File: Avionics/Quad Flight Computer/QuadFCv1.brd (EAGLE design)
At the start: 63.5 x 38.1 mm, 111 parts, among them J1 10104111_MICROUSBAB, J2 1050270001, SW1 2-1437565-9, U1 TM4C123GH6PZ, U2 74LVC4245APW, U3 ATMEGA32U2-MU, U4 SPI_PPM, U5 MPU-6000, U6 HMC5883LSMD, U7 MS5611-01BA, U8 74AUP1G19GW, U9 S25FL127S, X1 HWB, Y1 32.768KHZ, Y2 AWSCR-20.00CW-T, Y3 PRQC16.00SR5010X000

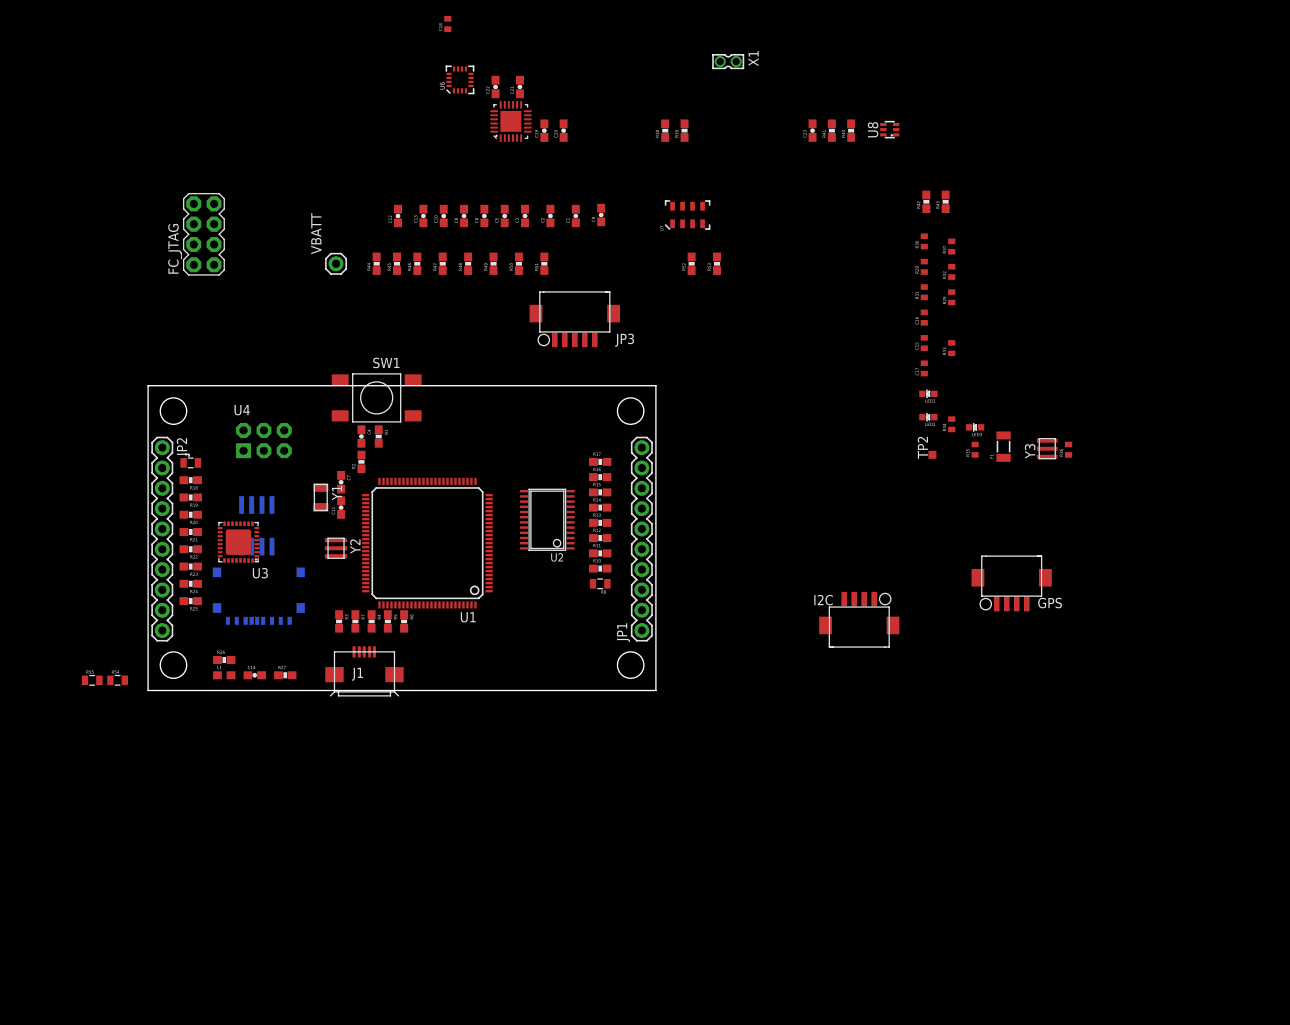
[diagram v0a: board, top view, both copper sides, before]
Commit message: Replaced all parts with 0402 packages to save board space.
I'm gonna need a smaller tweezers...
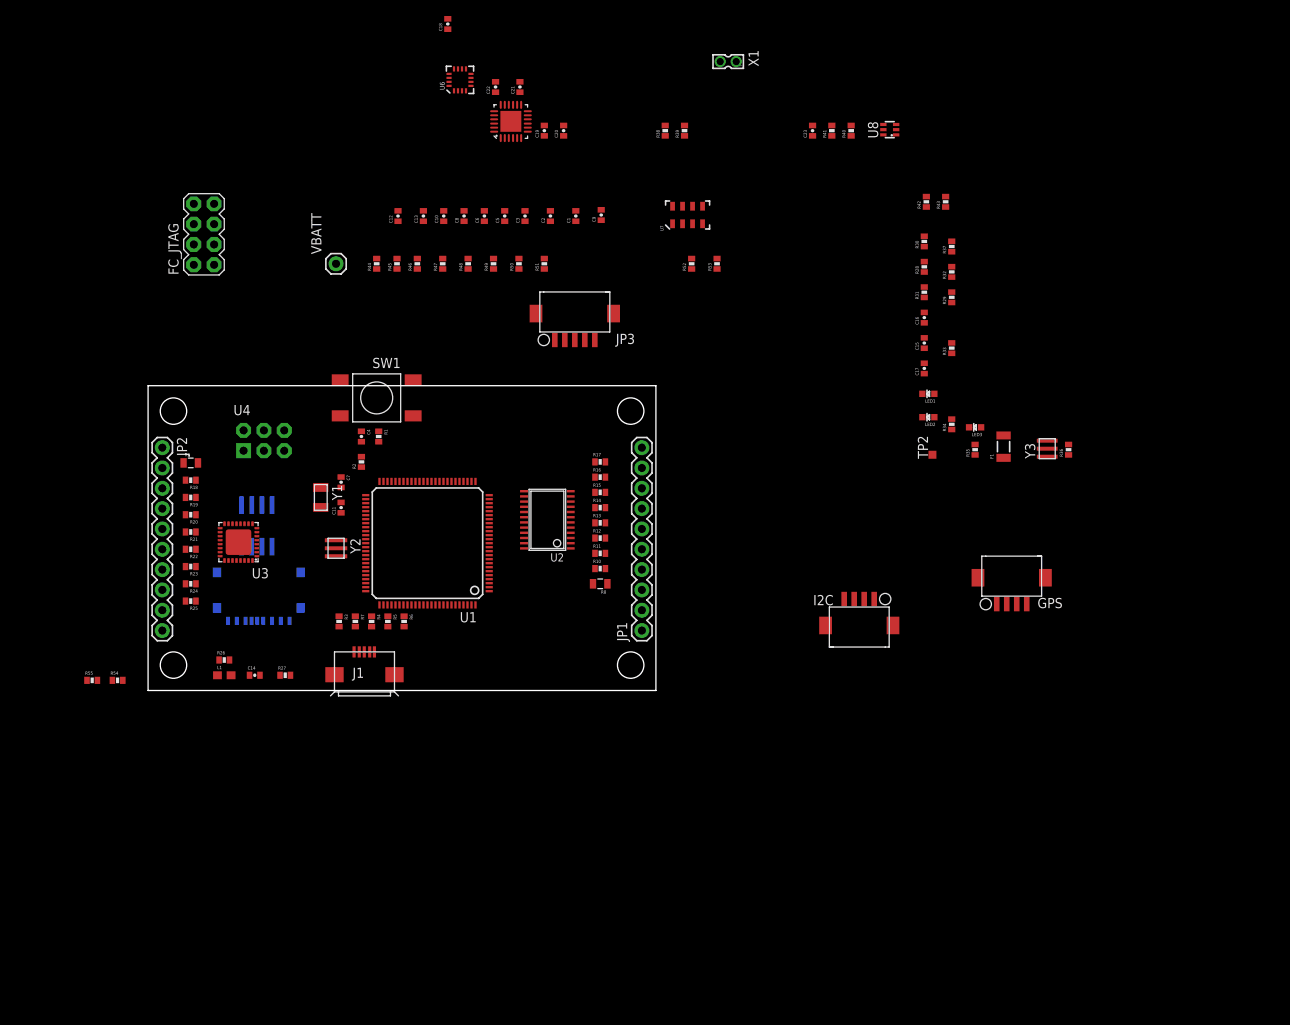
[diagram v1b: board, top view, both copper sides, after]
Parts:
- C1, C10, C11, C12, C13, C19, C2, C20, C21, C22, C23, C3, C4, C5, C6, C7, C8, C9: device SparkFun-Capacitors:0603-CAP -> SparkFun-Capacitors:0402-CAP
- C14: device SparkFun-Passives:0603-CAP -> SparkFun-Capacitors:0402-CAP
- C15, C16, C17, C18: device SparkFun:C0402 -> SparkFun-Capacitors:0402-CAP
- R1, R10, R11, R12, R13, R14, R15, R16, R17, R18, R19, R2, R20, R21, R22, R23, R24, R25, R26, R27, R38, R39, R40, R41: device SparkFun-Resistors:0603-RES -> SparkFun-Resistors:0402-RES
- R28, R29, R30, R31, R32, R33, R34, R35, R36, R37: device SparkFun:C0402 -> SparkFun-Resistors:0402-RES
- R3, R4, R42, R43, R44, R45, R46, R47, R48, R49, R5, R50, R51, R52, R53, R6, R7: device Shared Libraries:0603-RES -> SparkFun-Resistors:0402-RES
- R54, R55: value DNP -> 0; device SparkFun-Resistors:0805 -> SparkFun-Resistors:0402-RES
- R8, R9: value 0 -> DNP

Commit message: Added power management circuitry
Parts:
- added C24: 1uF, SparkFun-Capacitors:0603-CAP
- added C25, C26: 1u, SparkFun-Capacitors:0402-CAP
- added Q1, Q2, Q3: DMP2035U, Shared Libraries:SOT23
- added R56: 470K, Shared Libraries:0402-RES
- added U10: LTC4412, Shared Libraries:SOT23-6
- added U11: AP7215-33YG-13, Shared Libraries:SOT89
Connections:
- new net N$41: Q2.1, U10.5
- new net N$42: F1.1, Q1.3, Q3.2
- new net USB_EPEN: Q3.1
- new net USB_POWER_CONN_L: Q1.1, R56.1, U10.4
- new net VBUS: F1.2
- net 3.3V: now also C26.1, U11.3
- net 5V: now also C24.2, C25.1, Q1.2, Q2.2, R56.2, U10.6, U11.2, U11.2@1
- net 5VBATT: now also Q2.3, Q3.3, U10.1
- net GND: now also C24.1, C25.2, C26.2, U10.2, U10.3, U11.1
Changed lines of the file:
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@@
 <element name="R54" library="SparkFun-Resistors" package="0402-RES" value="0" x="-3.81" y="1.27"/>
 <element name="R55" library="SparkFun-Resistors" package="0402-RES" value="0" x="-6.985" y="1.27"/>
+<element name="Q1" library="Shared Libraries" package="SOT23" value="DMP2035U" x="-5.715" y="-4.445"/>
+<element name="Q2" library="Shared Libraries" package="SOT23" value="DMP2035U" x="-5.715" y="-12.065"/>
+<element name="Q3" library="Shared Libraries" package="SOT23" value="DMP2035U" x="-5.715" y="-19.685"/>
+<element name="U10" library="Shared Libraries" package="SOT23-6" value="LTC4412" x="-6.35" y="-26.67"/>
+<element name="R56" library="Shared Libraries" package="0402-RES" value="470K" x="-6.985" y="-31.115"/>
+<element name="C24" library="SparkFun-Capacitors" package="0603-CAP" value="1uF" x="-6.985" y="-33.655"/>
+<element name="U11" library="Shared Libraries" package="SOT89" value="AP7215-33YG-13" x="-13.97" y="-29.845"/>
+<element name="C25" library="SparkFun-Capacitors" package="0402-CAP" value="1u" x="-15.24" y="-36.83"/>
+<element name="C26" library="SparkFun-Capacitors" package="0402-CAP" value="1u" x="-15.24" y="-39.37"/>
 </elements>
 <signals>
@@
 <contactref element="R53" pad="2"/>
 <contactref element="I2C" pad="P1"/>
+<contactref element="U11" pad="3"/>
+<contactref element="C26" pad="1"/>
 <wire x1="83.058" y1="69.327" x2="91.91" y2="70.104" width="0" layer="19" extent="1-1"/>
 <wire x1="97.282" y1="61.737" x2="91.91" y2="70.104" width="0" layer="19" extent="1-1"/>
@@
 <wire x1="10.375" y1="1.905" x2="10.175" y2="3.81" width="0" layer="19" extent="1-1"/>
 <wire x1="5.715" y1="55.753" x2="34.417" y2="58.659" width="0" layer="19" extent="1-1"/>
+<wire x1="-12.471" y1="-31.826" x2="10.375" y2="1.905" width="0" layer="19" extent="1-1"/>
+<wire x1="-15.89" y1="-39.37" x2="-12.471" y2="-31.826" width="0" layer="19" extent="1-1"/>
 <wire x1="90.765" y1="11.43" x2="46.9932" y2="17.761" width="0" layer="19" extent="1-1"/>
 </signal>
@@
 <contactref element="GPS" pad="P4"/>
 <contactref element="I2C" pad="P4"/>
+<contactref element="U10" pad="2"/>
+<contactref element="U10" pad="3"/>
+<contactref element="C24" pad="1"/>
+<contactref element="C26" pad="2"/>
+<contactref element="U11" pad="1"/>
+<contactref element="C25" pad="2"/>
 <wire x1="83.058" y1="70.627" x2="93.51" y2="70.104" width="0" layer="19" extent="1-1"/>
 <wire x1="71.517" y1="78.613" x2="83.058" y2="70.627" width="0" layer="19" extent="1-1"/>
@@
 <wire x1="5.715" y1="60.833" x2="31.242" y2="59.959" width="0" layer="19" extent="1-1"/>
 <wire x1="5.715" y1="58.293" x2="5.715" y2="60.833" width="0" layer="19" extent="1-1"/>
+<wire x1="-5.4" y1="-27.82" x2="12.685" y2="1.905" width="0" layer="19" extent="1-1"/>
+<wire x1="-6.35" y1="-27.82" x2="-5.4" y2="-27.82" width="0" layer="19" extent="1-1"/>
+<wire x1="-7.835" y1="-33.655" x2="-6.35" y2="-27.82" width="0" layer="19" extent="1-1"/>
+<wire x1="-14.59" y1="-36.83" x2="-7.835" y2="-33.655" width="0" layer="19" extent="1-1"/>
+<wire x1="-14.59" y1="-39.37" x2="-14.59" y2="-36.83" width="0" layer="19" extent="1-1"/>
+<wire x1="-15.469" y1="-31.826" x2="-14.59" y2="-36.83" width="0" layer="19" extent="1-1"/>
 </signal>
 <signal name="5V">
@@
 <contactref element="R52" pad="2"/>
 <contactref element="R54" pad="2"/>
+<contactref element="Q2" pad="2"/>
+<contactref element="Q1" pad="2"/>
+<contactref element="U10" pad="6"/>
+<contactref element="R56" pad="2"/>
+<contactref element="C24" pad="2"/>
+<contactref element="C25" pad="1"/>
+<contactref element="U11" pad="2@1"/>
+<contactref element="U11" pad="2"/>
 <wire x1="100.457" y1="42.149" x2="100.457" y2="49.799" width="0" layer="19" extent="1-1"/>
 <wire x1="97.028" y1="42.784" x2="100.457" y2="42.149" width="0" layer="19" extent="1-1"/>
@@
 <wire x1="11.938" y1="32.512" x2="13.603" y2="18.292" width="0" layer="19" extent="1-1"/>
 <wire x1="-3.16" y1="1.27" x2="13.053" y2="16.242" width="0" layer="19" extent="1-1"/>
+<wire x1="-4.765" y1="-5.545" x2="-3.16" y2="1.27" width="0" layer="19" extent="1-1"/>
+<wire x1="-4.765" y1="-13.165" x2="-4.765" y2="-5.545" width="0" layer="19" extent="1-1"/>
+<wire x1="-7.3" y1="-25.52" x2="-4.765" y2="-13.165" width="0" layer="19" extent="1-1"/>
+<wire x1="-6.335" y1="-31.115" x2="-7.3" y2="-25.52" width="0" layer="19" extent="1-1"/>
+<wire x1="-6.135" y1="-33.655" x2="-6.335" y2="-31.115" width="0" layer="19" extent="1-1"/>
+<wire x1="-13.97" y1="-28.905" x2="-7.3" y2="-25.52" width="0" layer="19" extent="1-1"/>
+<wire x1="-13.97" y1="-31.572" x2="-13.97" y2="-28.905" width="0" layer="19" extent="1-1"/>
+<wire x1="-15.89" y1="-36.83" x2="-13.97" y2="-31.572" width="0" layer="19" extent="1-1"/>
 </signal>
 <signal name="N$1">
@@
 <contactref element="R9" pad="2"/>
 <contactref element="R55" pad="2"/>
+<contactref element="U10" pad="1"/>
+<contactref element="Q2" pad="3"/>
+<contactref element="Q3" pad="3"/>
 <wire x1="-6.335" y1="1.27" x2="6.234" y2="28.448" width="0" layer="19" extent="1-1"/>
+<wire x1="-5.715" y1="-10.965" x2="-6.335" y2="1.27" width="0" layer="19" extent="1-1"/>
+<wire x1="-5.715" y1="-18.585" x2="-5.715" y2="-10.965" width="0" layer="19" extent="1-1"/>
+<wire x1="-7.3" y1="-27.82" x2="-5.715" y2="-18.585" width="0" layer="19" extent="1-1"/>
+</signal>
+<signal name="N$41">
+<contactref element="Q2" pad="1"/>
+<contactref element="U10" pad="5"/>
+<wire x1="-6.665" y1="-13.165" x2="-6.35" y2="-25.52" width="0" layer="19" extent="1-1"/>
+</signal>
+<signal name="USB_POWER_CONN_L">
+<contactref element="U10" pad="4"/>
+<contactref element="Q1" pad="1"/>
+<contactref element="R56" pad="1"/>
+<wire x1="-5.4" y1="-25.52" x2="-7.635" y2="-31.115" width="0" layer="19" extent="1-1"/>
+<wire x1="-6.665" y1="-5.545" x2="-5.4" y2="-25.52" width="0" layer="19" extent="1-1"/>
+</signal>
+<signal name="USB_EPEN">
+<contactref element="Q3" pad="1"/>
+</signal>
+<signal name="VBUS">
+<contactref element="F1" pad="2"/>
+</signal>
+<signal name="N$42">
+<contactref element="F1" pad="1"/>
+<contactref element="Q1" pad="3"/>
+<contactref element="Q3" pad="2"/>
+<wire x1="-5.715" y1="-3.345" x2="106.934" y2="29.08" width="0" layer="19" extent="1-1"/>
+<wire x1="-4.765" y1="-20.785" x2="-5.715" y2="-3.345" width="0" layer="19" extent="1-1"/>
 </signal>
 </signals>

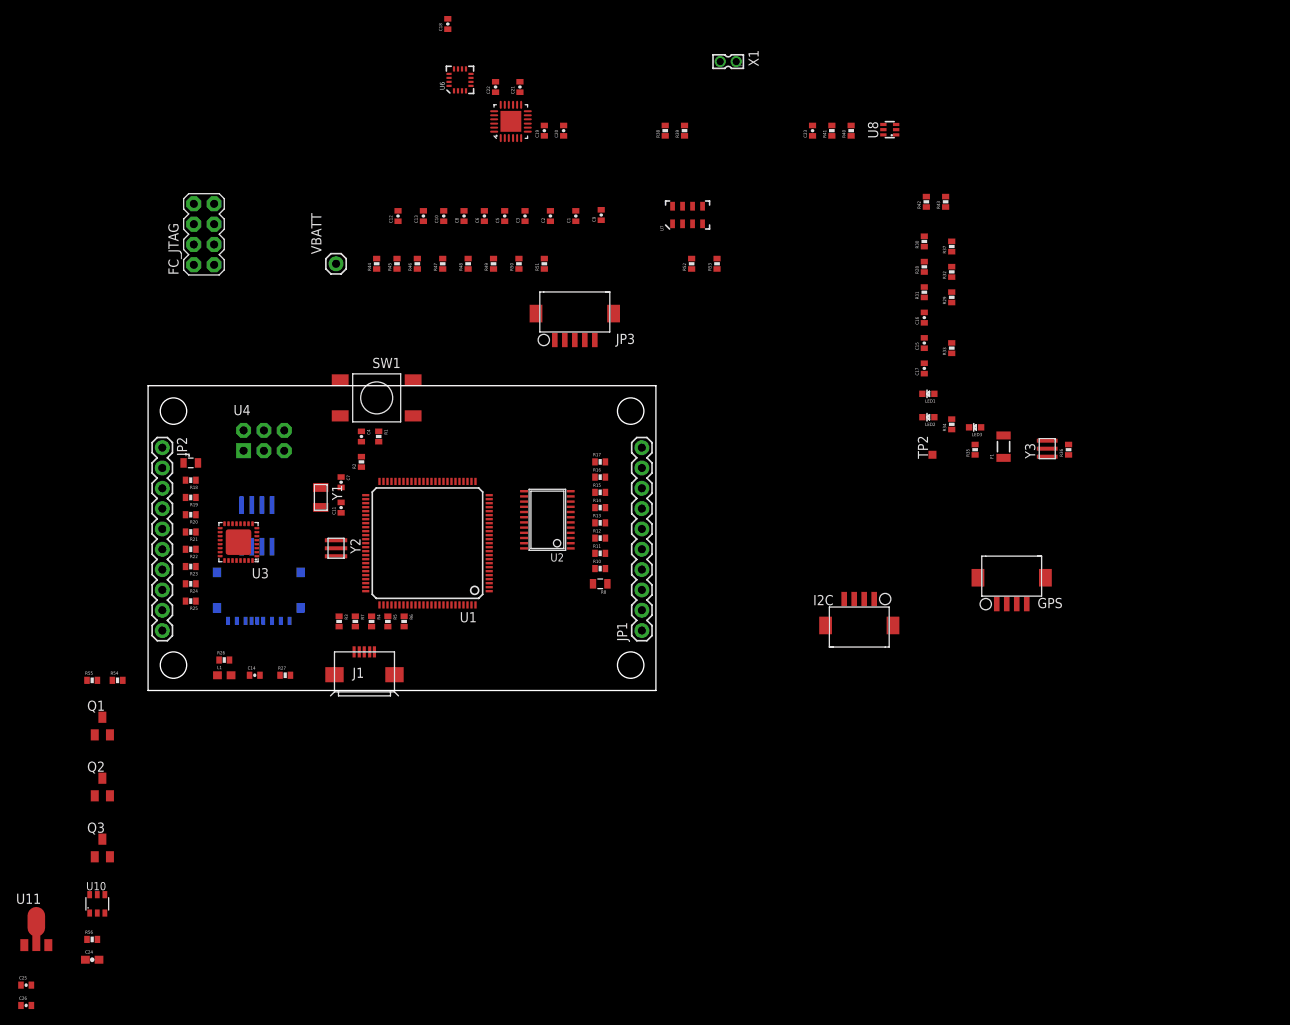
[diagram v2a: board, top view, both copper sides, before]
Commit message: Changed form factor of FC to be 1.95"x1.95" to be compliant with the power distribution board. Makes stacking and interconnectivity simpler.
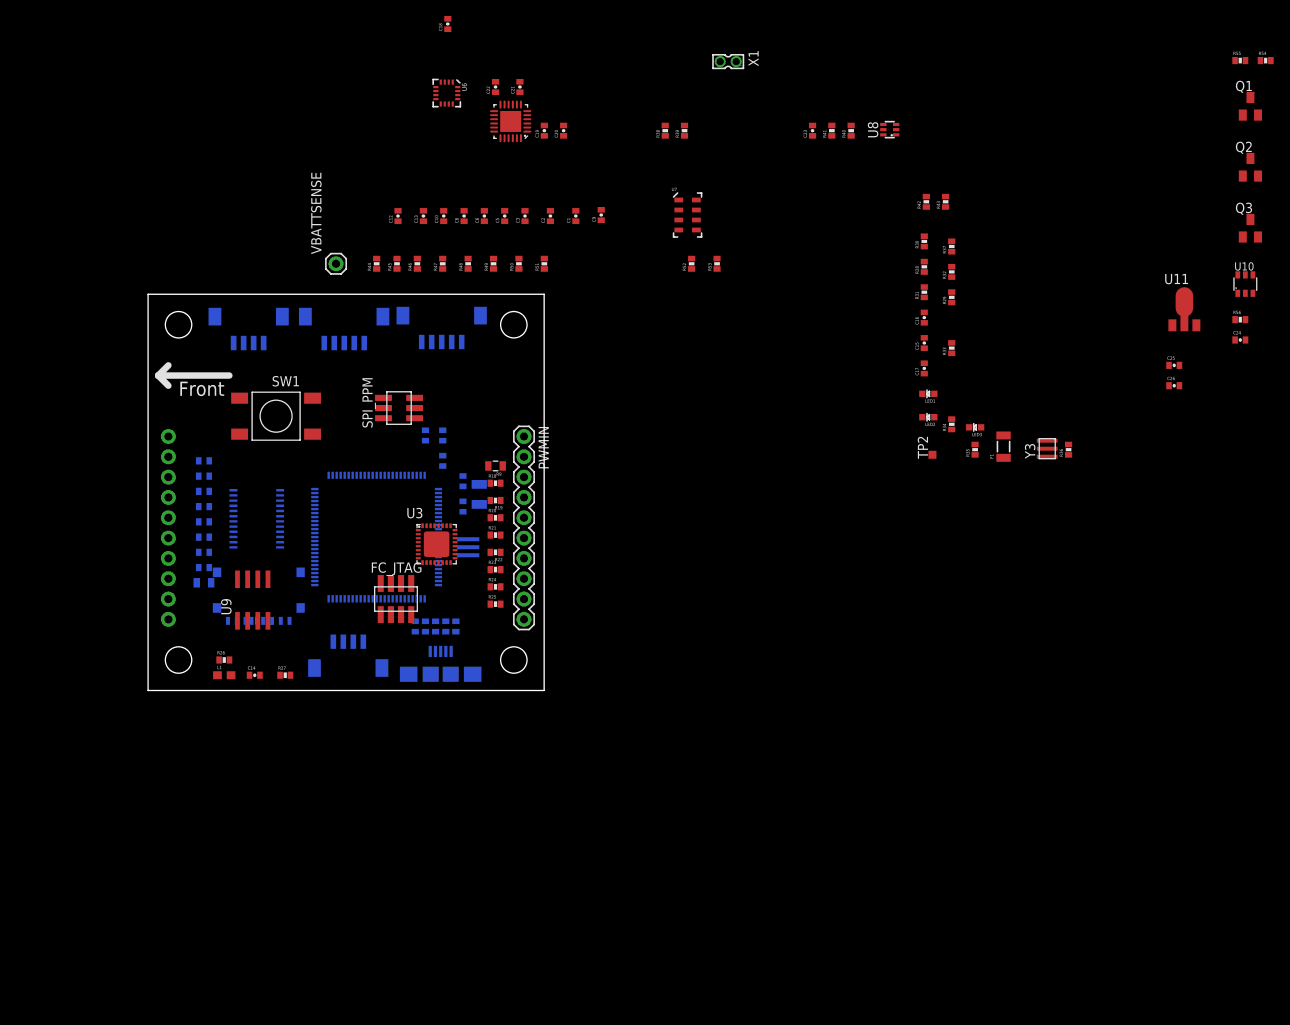
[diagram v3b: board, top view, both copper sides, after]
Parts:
- removed J1: 10104111_MICROUSBAB, Shared Libraries:USB-AB-10104111
- removed JP1, JP2: M10", SparkFun-Connectors:1X10
- removed JP3: (no value), Shared Libraries:DF13_5POS
- removed U4: SPI_PPM, SparkFunv2:2X3-NS
- added ISENSE, RADIO1: (no value), Shared Libraries:DF13_5POS
- added PWMIN, PWMOUT: M10", SparkFun-Connectors:1X10
- added SPI_PPM: SPI_PPM, Shared Libraries:2X3_SMT_0.5
- added U12: (no value), SparkFun-Connectors:USB-AB-MICRO-SMD
- C24: device SparkFun-Capacitors:0603-CAP -> SparkFun-Capacitors:0402-CAP
- FC_JTAG: value M04X2 -> M04X2SMT-0.05; device SparkFun-Connectors:2X4 -> Shared Libraries:2X4_SMT-0.05
- moved C24 163.1 mm to (136.5, 43.8)
- moved C25 163.1 mm to (128.3, 40.6)
- moved C26 163.1 mm to (128.3, 38.1)
- moved R55 163.1 mm to (136.5, 78.7)
- moved R56 163.1 mm to (136.5, 46.4)
- moved Q1 163.1 mm to (137.8, 73.0)
- moved Q2 163.1 mm to (137.8, 65.4)
- moved Q3 163.1 mm to (137.8, 57.8)
- moved R54 163.1 mm to (139.7, 78.7)
- moved U10 163.1 mm to (137.2, 50.8)
- moved U11 163.1 mm to (129.5, 47.6)
- moved GPS 99.6 mm to (13.2, 46.0), flipped to the bottom
- moved I2C 65.4 mm to (24.4, 3.56), flipped to the bottom
- moved FC_JTAG 51.2 mm to (30.4, 11.4), turned to 0 degrees
- moved R10 49.5 mm to (6.99, 15.4), flipped to the bottom
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- renumbered VBATT to VBATTSENSE
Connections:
- new net RADIO_UART_RX: RADIO1.P3
- new net RADIO_UART_TX: RADIO1.P2
- net 3.3V: now also RADIO1.P4
- net 5V: now also RADIO1.P1, SPI_PPM.2; no longer U4.2
- net GND: now also PWMIN.2, PWMOUT.2, RADIO1.P5, SPI_PPM.6, U12.GND; no longer J1.5, J1.GND@1, J1.GND@2, JP1.1, JP2.1, U4.6
- net N$1: now also PWMIN.3; no longer JP2.3
- net N$10: now also PWMOUT.4; no longer JP1.4
- net N$11: now also PWMOUT.5; no longer JP1.5
- net N$12: now also PWMOUT.6; no longer JP1.6
- net N$13: now also PWMOUT.7; no longer JP1.7
- net N$14: now also PWMOUT.8; no longer JP1.8
- net N$15: now also PWMOUT.9; no longer JP1.9
- net N$16: now also PWMOUT.10; no longer JP1.10
- net N$2: now also PWMIN.4; no longer JP2.4
- net N$23: now also PWMIN.1; no longer JP2.2
- net N$26: now also PWMOUT.1; no longer JP1.2
- net N$27: now also U12.ID; no longer J1.4
- net N$28: now also U12.D-; no longer J1.2
- net N$29: now also U12.D+; no longer J1.3
- net N$3: now also PWMIN.5; no longer JP2.5
- net N$4: now also PWMIN.6; no longer JP2.6
- net N$44: now also ISENSE.P1; no longer JP3.P1
- net N$45: now also ISENSE.P2; no longer JP3.P2
- net N$46: now also ISENSE.P3; no longer JP3.P3
- net N$47: now also ISENSE.P4; no longer JP3.P4
- net N$48: now also ISENSE.P5; no longer JP3.P5
- net N$5: now also PWMIN.7; no longer JP2.7
- net N$6: now also PWMIN.8; no longer JP2.8
- net N$7: now also PWMIN.9; no longer JP2.9
- net N$8: now also PWMIN.10; no longer JP2.10
- net N$9: now also PWMOUT.3; no longer JP1.3
- net PPM_RST: now also SPI_PPM.5; no longer U4.5
- net PWMIN2: now also SPI_PPM.3; no longer U4.3
- net PWMIN3: now also SPI_PPM.4; no longer U4.4
- net PWMIN4: now also SPI_PPM.1; no longer U4.1
- net VUSB: now also U12.VBUS; no longer J1.1
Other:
- board size 63.5 x 38.1 mm -> 49.5 x 49.5 mm
- board text added: "Front"
